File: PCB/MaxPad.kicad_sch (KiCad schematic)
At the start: 27 parts, among them J1 Conn_01x04_Pin, SW1 SW_Push, SW10 SW_Push, SW11 SW_Push, SW12 SW_Push, SW13 RotaryEncoder, SW2 SW_Push, SW3 SW_Push, SW4 SW_Push, SW5 SW_Push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

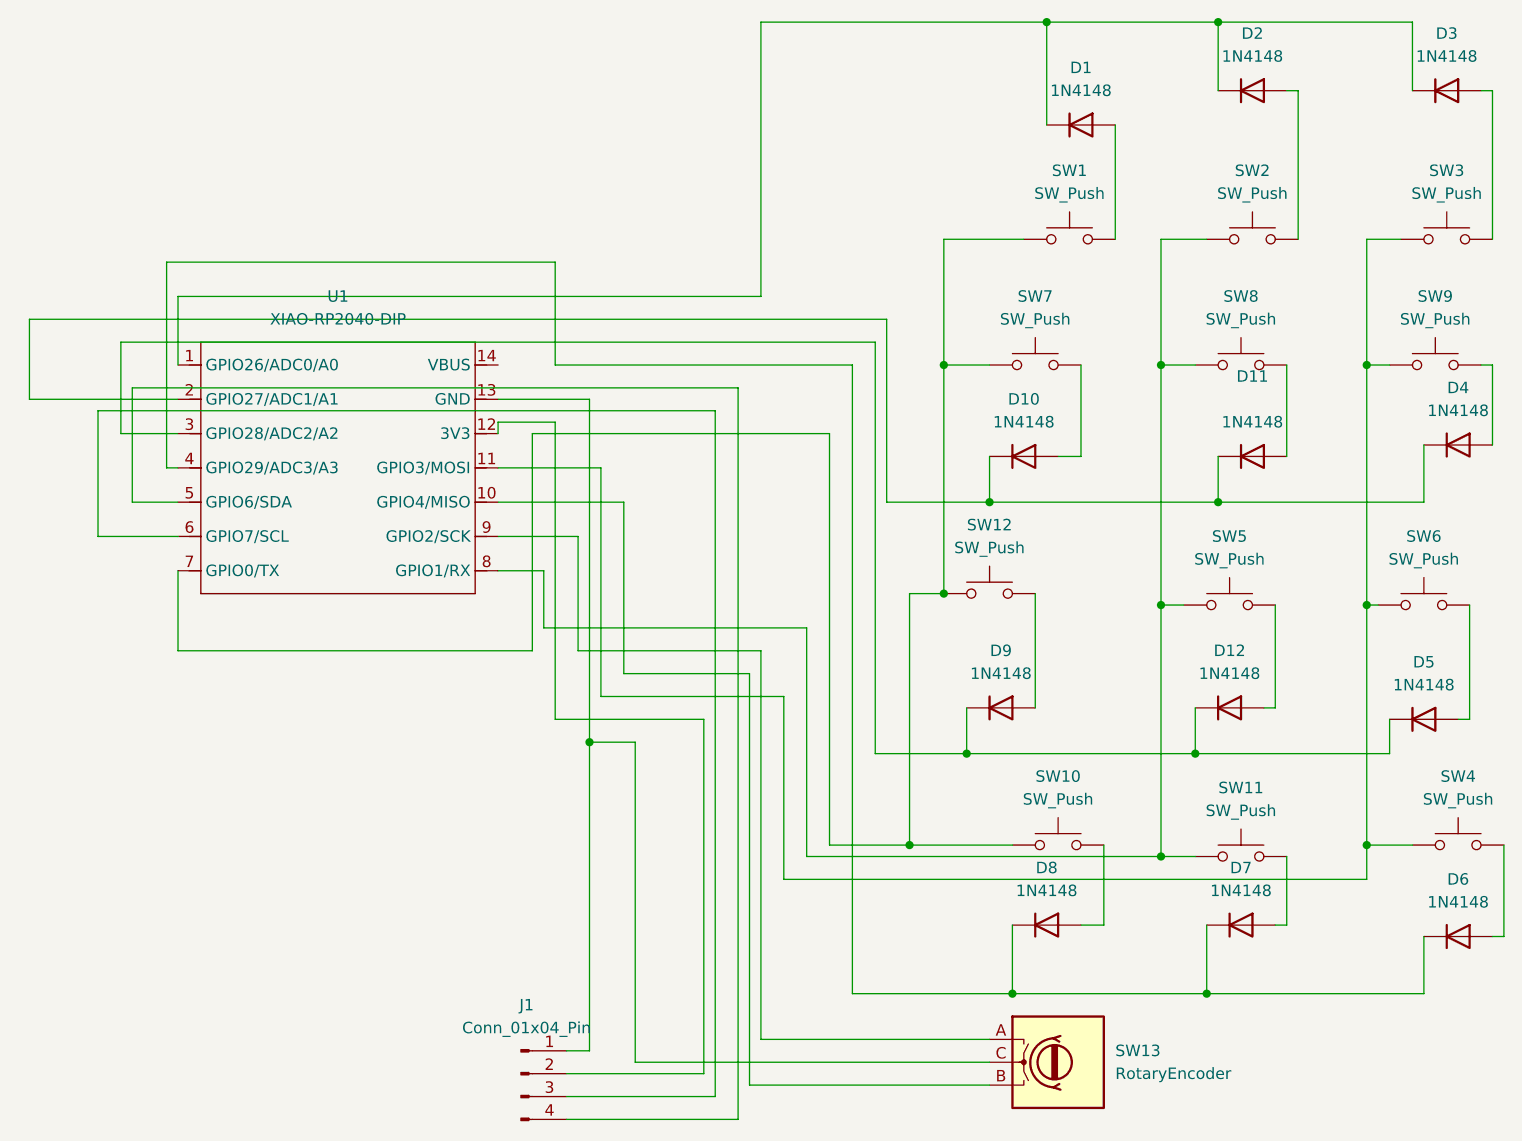
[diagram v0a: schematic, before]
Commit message: Adding sufficient gap and using labels in schematic
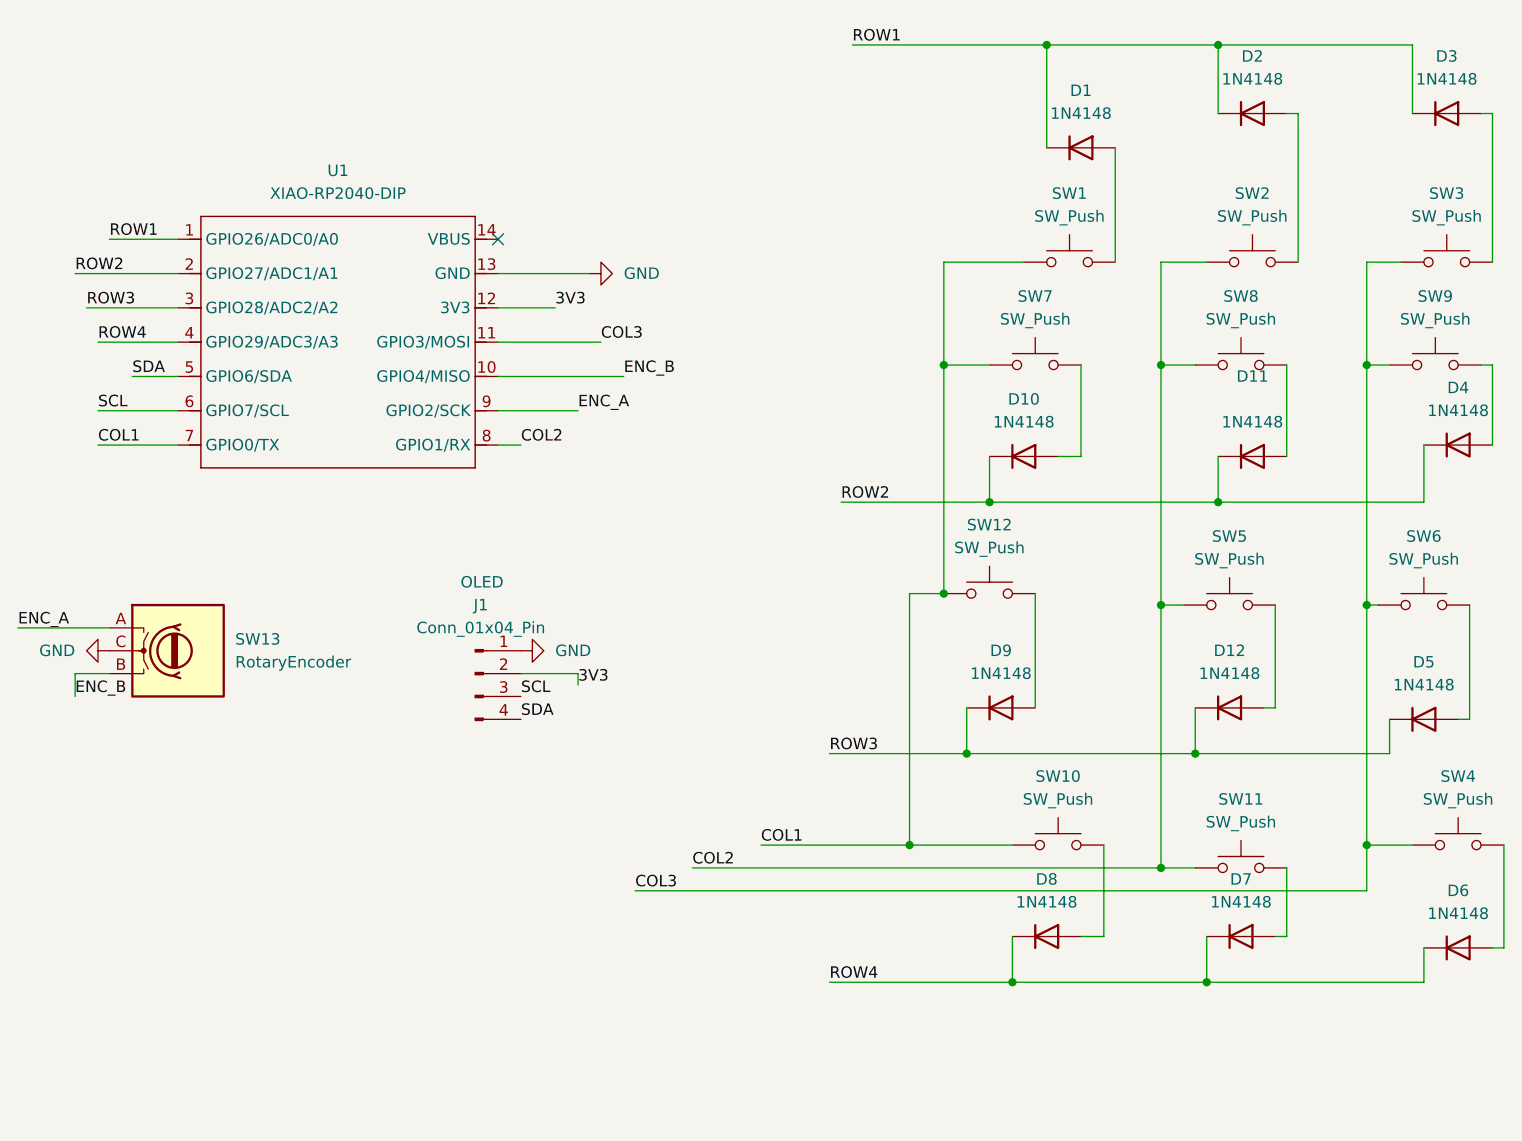
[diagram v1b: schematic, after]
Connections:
- net ROW4: now reaches D6.1 (K), D7.1 (K), D8.1 (K), U1.4 (GPIO29/ADC3/A3)
- net COL2: now reaches SW11.1, SW2.1, SW5.1, SW8.1, U1.8 (GPIO1/RX)
- net ROW1: now reaches D1.1 (K), D2.1 (K), D3.1 (K), U1.1 (GPIO26/ADC0/A0)
- net ROW2: now reaches D10.1 (K), D11.1 (K), D4.1 (K), U1.2 (GPIO27/ADC1/A1)
- net COL3: now reaches SW3.1, SW4.1, SW6.1, SW9.1, U1.11 (GPIO3/MOSI)
- net COL1: now reaches SW1.1, SW10.1, SW12.1, SW7.1, U1.7 (GPIO0/TX)
- net ENC_A: now reaches SW13.A, U1.9 (GPIO2/SCK)
- net ENC_B: now reaches SW13.B, U1.10 (GPIO4/MISO)
- net GND: now reaches J1.1 (Pin_1), SW13.C, U1.13 (GND)
- net 3V3: now reaches J1.2 (Pin_2), U1.12 (3V3)
- net ROW3: now reaches D12.1 (K), D5.1 (K), D9.1 (K), U1.3 (GPIO28/ADC2/A2)
- net SDA: now reaches J1.4 (Pin_4), U1.5 (GPIO6/SDA)
- net SCL: now reaches J1.3 (Pin_3), U1.6 (GPIO7/SCL)
- no-connect marks 0 -> 1
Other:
- note added: "OLED"
- moved on the sheet: D1, D2, D3, D6, D7, D8, J1, SW1, SW11, SW13, SW2, SW3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
